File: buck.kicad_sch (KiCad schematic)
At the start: 40 parts, among them J7 Conn_01x02_Socket, Q3 BSC059N04LS6, Q4 BSC059N04LS6, U6 BQ24640

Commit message: Completed preliminary layout
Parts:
- gave numbers to parts that had none: 5
- renumbered C7 to C37, C8 to C38, C9 to C39, C10 to C40, C11 to C41, C12 to C42, C13 to C43, C14 to C44, C15 to C45, C16 to C46, C17 to C47, C18 to C48, C19 to C49, D2 to D4, D3 to D5, D4 to D6, D5 to D7, J7 to J29, L1 to L4, Q3 to Q4, Q4 to Q5, R19 to R36, R20 to R37, R21 to R38, R22 to R39, R23 to R40, R24 to R41, R25 to R42, R26 to R43, R27 to R44, R28 to R45, R29 to R46, R30 to R47, R31 to R48, U6 to U15
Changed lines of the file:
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@@
 		(on_board yes)
 		(dnp no)
-		(property "Reference" "D3"
+		(property "Reference" "D5"
 			(at 86.36 96.8376 90)
 			(effects
@@
 		(dnp no)
 		(fields_autoplaced yes)
-		(property "Reference" "R22"
+		(property "Reference" "R39"
 			(at 234.95 73.6599 0)
 			(effects
@@
 		(dnp no)
 		(fields_autoplaced yes)
-		(property "Reference" "#PWR037"
+		(property "Reference" "#PWR098"
 			(at 193.04 86.36 0)
 			(effects
@@
 		(on_board yes)
 		(dnp no)
-		(property "Reference" "C12"
+		(property "Reference" "C42"
 			(at 208.28 73.6599 0)
 			(effects
@@
 		(on_board yes)
 		(dnp no)
-		(property "Reference" "Q3"
+		(property "Reference" "Q4"
 			(at 154.94 60.96 90)
 			(effects
@@
 		(dnp no)
 		(fields_autoplaced yes)
-		(property "Reference" "R30"
+		(property "Reference" "R47"
 			(at 228.6 135.8899 0)
 			(effects
@@
 		(dnp no)
 		(fields_autoplaced yes)
-		(property "Reference" "#PWR042"
+		(property "Reference" "#PWR0103"
 			(at 95.25 102.87 0)
 			(effects
@@
 		(on_board yes)
 		(dnp no)
-		(property "Reference" "D5"
+		(property "Reference" "D7"
 			(at 49.784 128.524 0)
 			(effects
@@
 		(dnp no)
 		(fields_autoplaced yes)
-		(property "Reference" "#PWR045"
+		(property "Reference" "#PWR0106"
 			(at 123.19 151.13 0)
 			(effects
@@
 		(dnp no)
 		(fields_autoplaced yes)
-		(property "Reference" "U6"
+		(property "Reference" "U15"
 			(at 67.31 80.01 0)
 			(effects
@@
 		(dnp no)
 		(fields_autoplaced yes)
-		(property "Reference" "#PWR044"
+		(property "Reference" "#PWR0105"
 			(at 226.06 148.59 0)
 			(effects
@@
 		(on_board yes)
 		(dnp no)
-		(property "Reference" "R20"
+		(property "Reference" "R37"
 			(at 121.412 59.182 90)
 			(effects
@@
 		(on_board yes)
 		(dnp no)
-		(property "Reference" "C13"
+		(property "Reference" "C43"
 			(at 219.71 73.6599 0)
 			(effects
@@
 		(dnp no)
 		(fields_autoplaced yes)
-		(property "Reference" "R19"
+		(property "Reference" "R36"
 			(at 68.58 33.02 90)
 			(effects
@@
 		(on_board yes)
 		(dnp no)
-		(property "Reference" "R27"
+		(property "Reference" "R44"
 			(at 31.75 128.27 90)
 			(effects
@@
 		(on_board yes)
 		(dnp no)
-		(property "Reference" "C18"
+		(property "Reference" "C48"
 			(at 97.79 92.7162 0)
 			(effects
@@
 		(on_board yes)
 		(dnp no)
-		(property "Reference" "D2"
+		(property "Reference" "D4"
 			(at 52.3876 36.83 90)
 			(effects
@@
 		(dnp no)
 		(fields_autoplaced yes)
-		(property "Reference" "R25"
+		(property "Reference" "R42"
 			(at 246.38 88.8999 0)
 			(effects
@@
 		(dnp no)
 		(fields_autoplaced yes)
-		(property "Reference" "#PWR043"
+		(property "Reference" "#PWR0104"
 			(at 67.31 135.89 0)
 			(effects
@@
 		(on_board yes)
 		(dnp no)
-		(property "Reference" "Q4"
+		(property "Reference" "Q5"
 			(at 154.94 77.47 90)
 			(effects
@@
 		(on_board yes)
 		(dnp no)
-		(property "Reference" "C9"
+		(property "Reference" "C39"
 			(at 38.1 42.2909 0)
 			(effects
@@
 		(on_board yes)
 		(dnp no)
-		(property "Reference" "D4"
+		(property "Reference" "D6"
 			(at 49.784 112.014 0)
 			(effects
@@
 		(on_board yes)
 		(dnp no)
-		(property "Reference" "C11"
+		(property "Reference" "C41"
 			(at 196.85 73.6599 0)
 			(effects
@@
 		(on_board yes)
 		(dnp no)
-		(property "Reference" "R23"
+		(property "Reference" "R40"
 			(at 121.412 75.692 90)
 			(effects
@@
 		(dnp yes)
 		(fields_autoplaced yes)
-		(property "Reference" "J7"
+		(property "Reference" "J29"
 			(at 245.11 135.8899 0)
 			(effects
@@
 		(on_board yes)
 		(dnp no)
-		(property "Reference" "C17"
+		(property "Reference" "C47"
 			(at 44.45 90.1762 0)
 			(effects
@@
 		(dnp no)
 		(fields_autoplaced yes)
-		(property "Reference" "R31"
+		(property "Reference" "R48"
 			(at 125.73 138.4299 0)
 			(effects
@@
 		(dnp no)
 		(fields_autoplaced yes)
-		(property "Reference" "R28"
+		(property "Reference" "R45"
 			(at 228.6 120.6499 0)
 			(effects
@@
 		(dnp no)
 		(fields_autoplaced yes)
-		(property "Reference" "R29"
+		(property "Reference" "R46"
 			(at 125.73 125.7299 0)
 			(effects
@@
 		(dnp no)
 		(fields_autoplaced yes)
-		(property "Reference" "#PWR040"
+		(property "Reference" "#PWR0101"
 			(at 46.99 100.33 0)
 			(effects
@@
 		(dnp no)
 		(fields_autoplaced yes)
-		(property "Reference" "L1"
+		(property "Reference" "L4"
 			(at 165.1 63.5 90)
 			(effects
@@
 		(dnp no)
 		(fields_autoplaced yes)
-		(property "Reference" "R21"
+		(property "Reference" "R38"
 			(at 179.07 63.5 90)
 			(effects
@@
 		(dnp no)
 		(fields_autoplaced yes)
-		(property "Reference" "#PWR041"
+		(property "Reference" "#PWR0102"
 			(at 232.41 101.6 0)
 			(effects
@@
 		(on_board yes)
 		(dnp yes)
-		(property "Reference" "TP?"
+		(property "Reference" "TP13"
 			(at 133.35 80.01 90)
 			(effects
@@
 		(on_board yes)
 		(dnp no)
-		(property "Reference" "C16"
+		(property "Reference" "C46"
 			(at 165.354 85.598 0)
 			(effects
@@
 		(on_board yes)
 		(dnp no)
-		(property "Reference" "C15"
+		(property "Reference" "C45"
 			(at 180.34 77.4699 0)
 			(effects
@@
 		(dnp no)
 		(fields_autoplaced yes)
-		(property "Reference" "R24"
+		(property "Reference" "R41"
 			(at 234.95 88.8999 0)
 			(effects
@@
 		(on_board yes)
 		(dnp yes)
-		(property "Reference" "TP?"
+		(property "Reference" "TP14"
 			(at 189.992 88.9 90)
 			(effects
@@
 		(on_board yes)
 		(dnp yes)
-		(property "Reference" "TP?"
+		(property "Reference" "TP10"
 			(at 133.35 53.34 90)
 			(effects
@@
 		(on_board yes)
 		(dnp no)
-		(property "Reference" "C8"
+		(property "Reference" "C38"
 			(at 142.24 39.3699 0)
 			(effects
@@
 		(dnp no)
 		(fields_autoplaced yes)
-		(property "Reference" "R26"
+		(property "Reference" "R43"
 			(at 31.75 111.76 90)
 			(effects
@@
 		(dnp no)
 		(fields_autoplaced yes)
-		(property "Reference" "#PWR035"
+		(property "Reference" "#PWR096"
 			(at 127 52.07 0)
 			(effects
@@
 		(on_board yes)
 		(dnp no)
-		(property "Reference" "C14"
+		(property "Reference" "C44"
 			(at 247.65 73.6599 0)
 			(effects
@@
 		(dnp no)
 		(fields_autoplaced yes)
-		(property "Reference" "#PWR036"
+		(property "Reference" "#PWR097"
 			(at 41.91 55.88 0)
 			(effects
@@
 		(dnp no)
 		(fields_autoplaced yes)
-		(property "Reference" "#PWR039"
+		(property "Reference" "#PWR0100"
 			(at 176.53 88.9 0)
 			(effects
@@
 		(dnp no)
 		(fields_autoplaced yes)
-		(property "Reference" "#PWR038"
+		(property "Reference" "#PWR099"
 			(at 148.59 88.9 0)
 			(effects
@@
 		(on_board yes)
 		(dnp no)
-		(property "Reference" "C19"
+		(property "Reference" "C49"
 			(at 81.28 101.6 0)
 			(effects
@@
 		(on_board yes)
 		(dnp no)
-		(property "Reference" "C10"
+		(property "Reference" "C40"
 			(at 80.01 43.1799 0)
 			(effects
@@
 		(dnp yes)
 		(fields_autoplaced yes)
-		(property "Reference" "TP?"
+		(property "Reference" "TP11"
 			(at 132.588 60.96 90)
 			(effects
@@
 		(dnp yes)
 		(fields_autoplaced yes)
-		(property "Reference" "TP?"
+		(property "Reference" "TP12"
 			(at 168.148 73.66 90)
 			(effects
@@
 		(on_board yes)
 		(dnp no)
-		(property "Reference" "C7"
+		(property "Reference" "C37"
 			(at 130.81 39.3699 0)
 			(effects

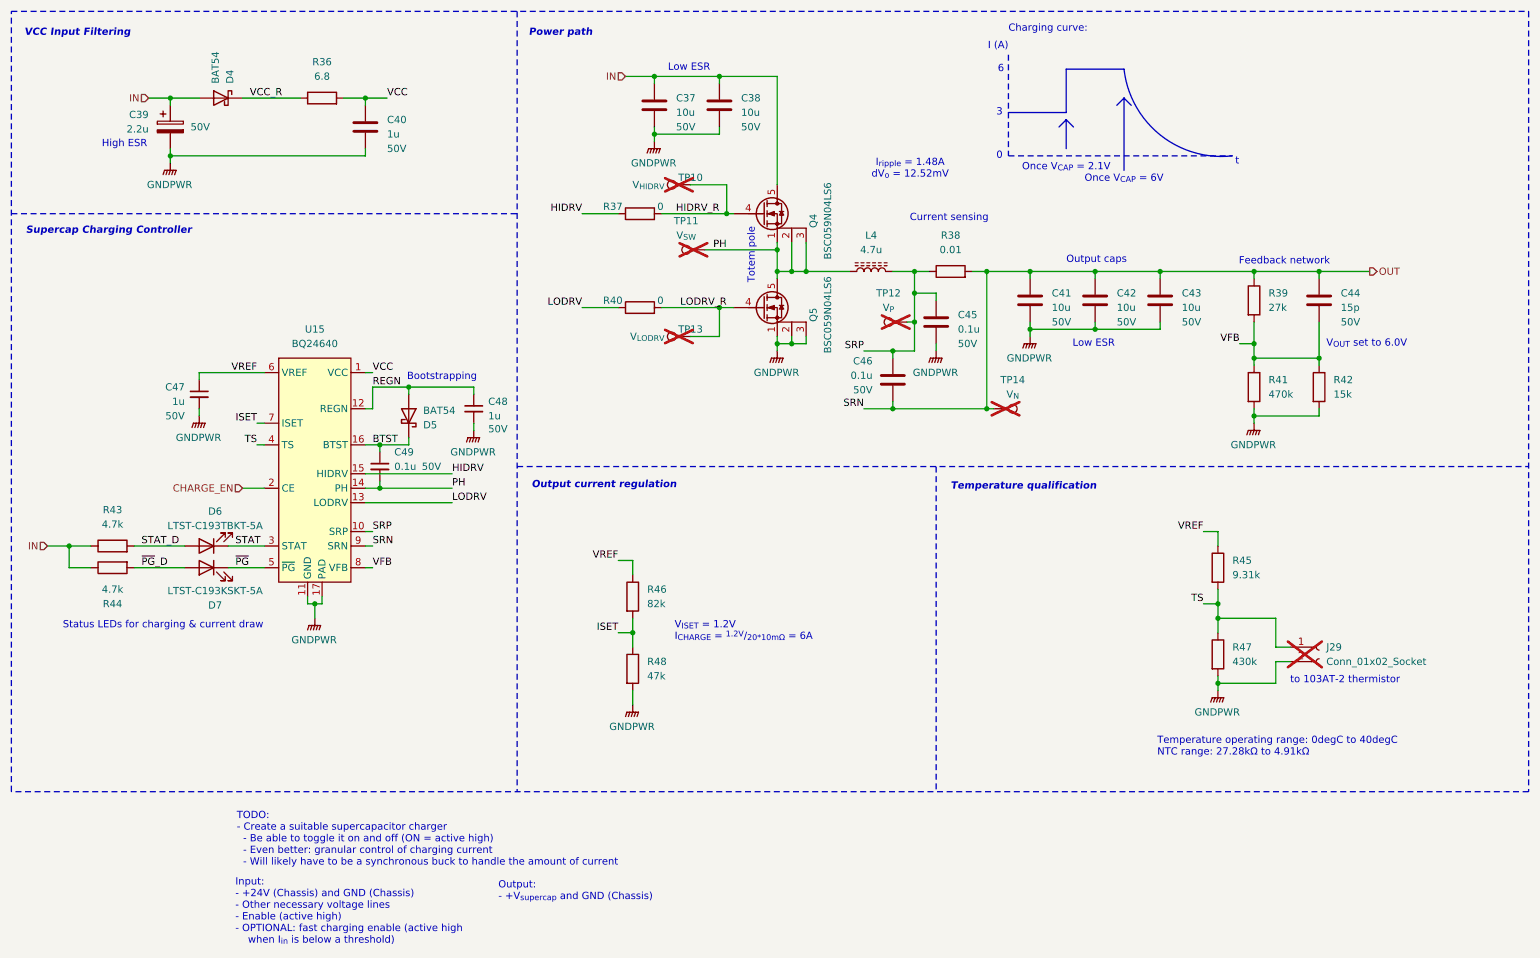
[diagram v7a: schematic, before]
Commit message: Completed layout for input buck test board
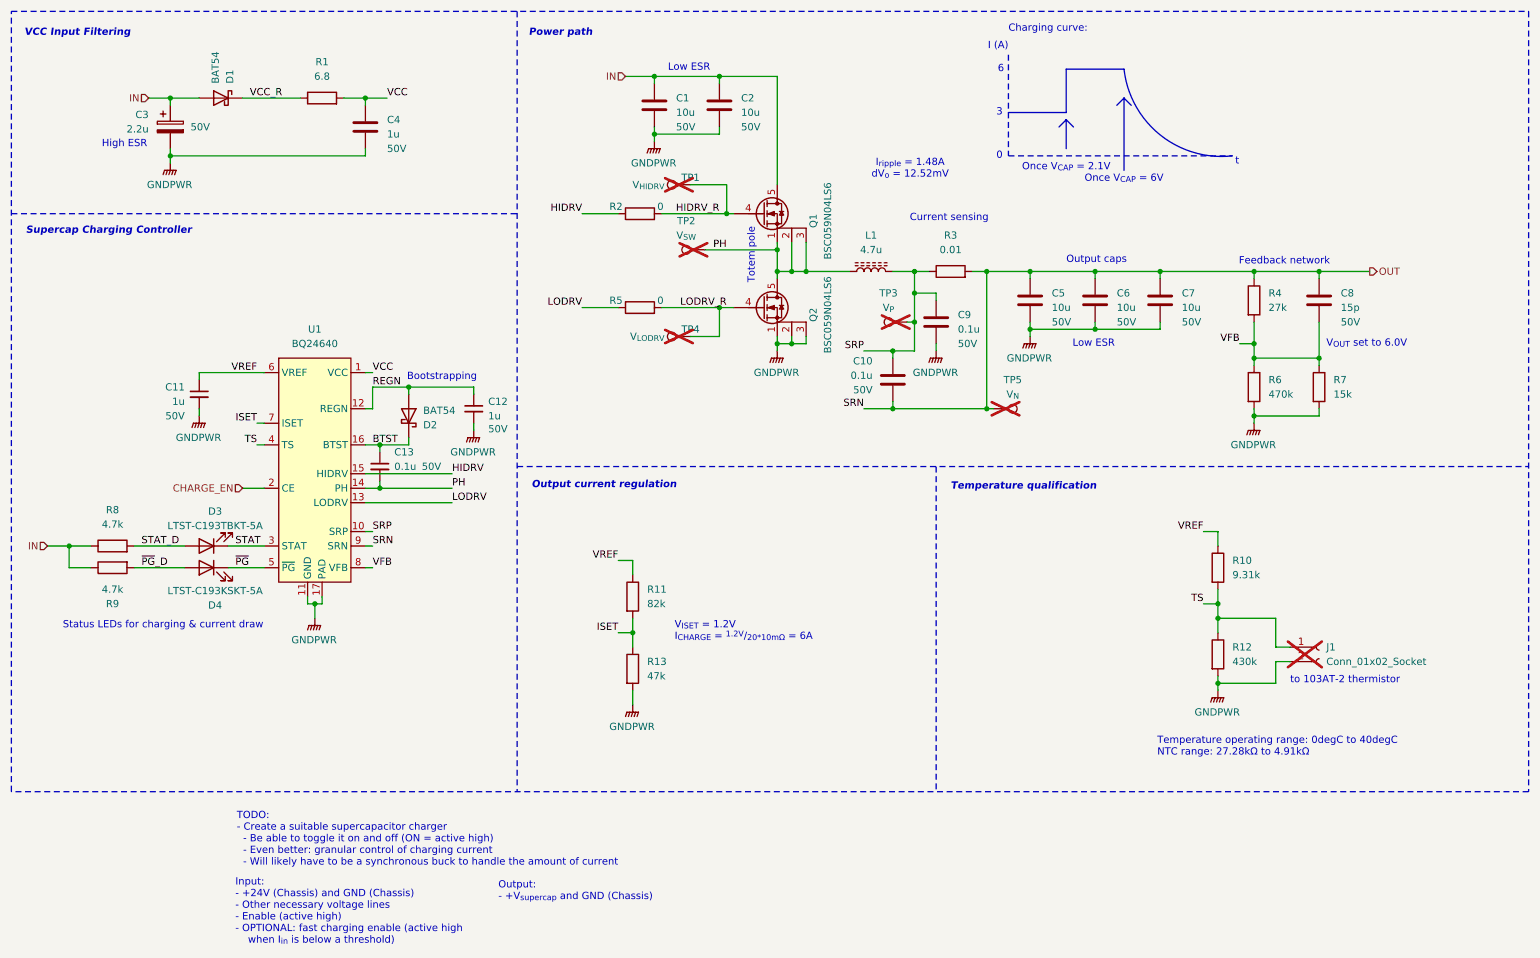
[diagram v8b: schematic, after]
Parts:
- J1: renamed from J29; footprint Connector_PinSocket_2.00mm:PinSocket_1x02_P2.00mm_Vertical -> Connector_PinSocket_2.54mm:PinSocket_1x02_P2.54mm_Vertical
- renumbered C37 to C1, C46 to C10, C47 to C11, C48 to C12, C49 to C13, C38 to C2, C39 to C3, C40 to C4, C41 to C5, C42 to C6, C43 to C7, C44 to C8, C45 to C9, D4 to D1, D5 to D2, D6 to D3, D7 to D4, L4 to L1, Q4 to Q1, Q5 to Q2, R36 to R1, R45 to R10, R46 to R11, R47 to R12, R48 to R13, R37 to R2, R38 to R3, R39 to R4, R40 to R5, R41 to R6, R42 to R7, R43 to R8, R44 to R9, TP10 to TP1, TP11 to TP2, TP12 to TP3, TP13 to TP4, TP14 to TP5, U15 to U1
